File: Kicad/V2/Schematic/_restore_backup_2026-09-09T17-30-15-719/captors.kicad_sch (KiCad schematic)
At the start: 7 parts, among them U2 TXS0104E

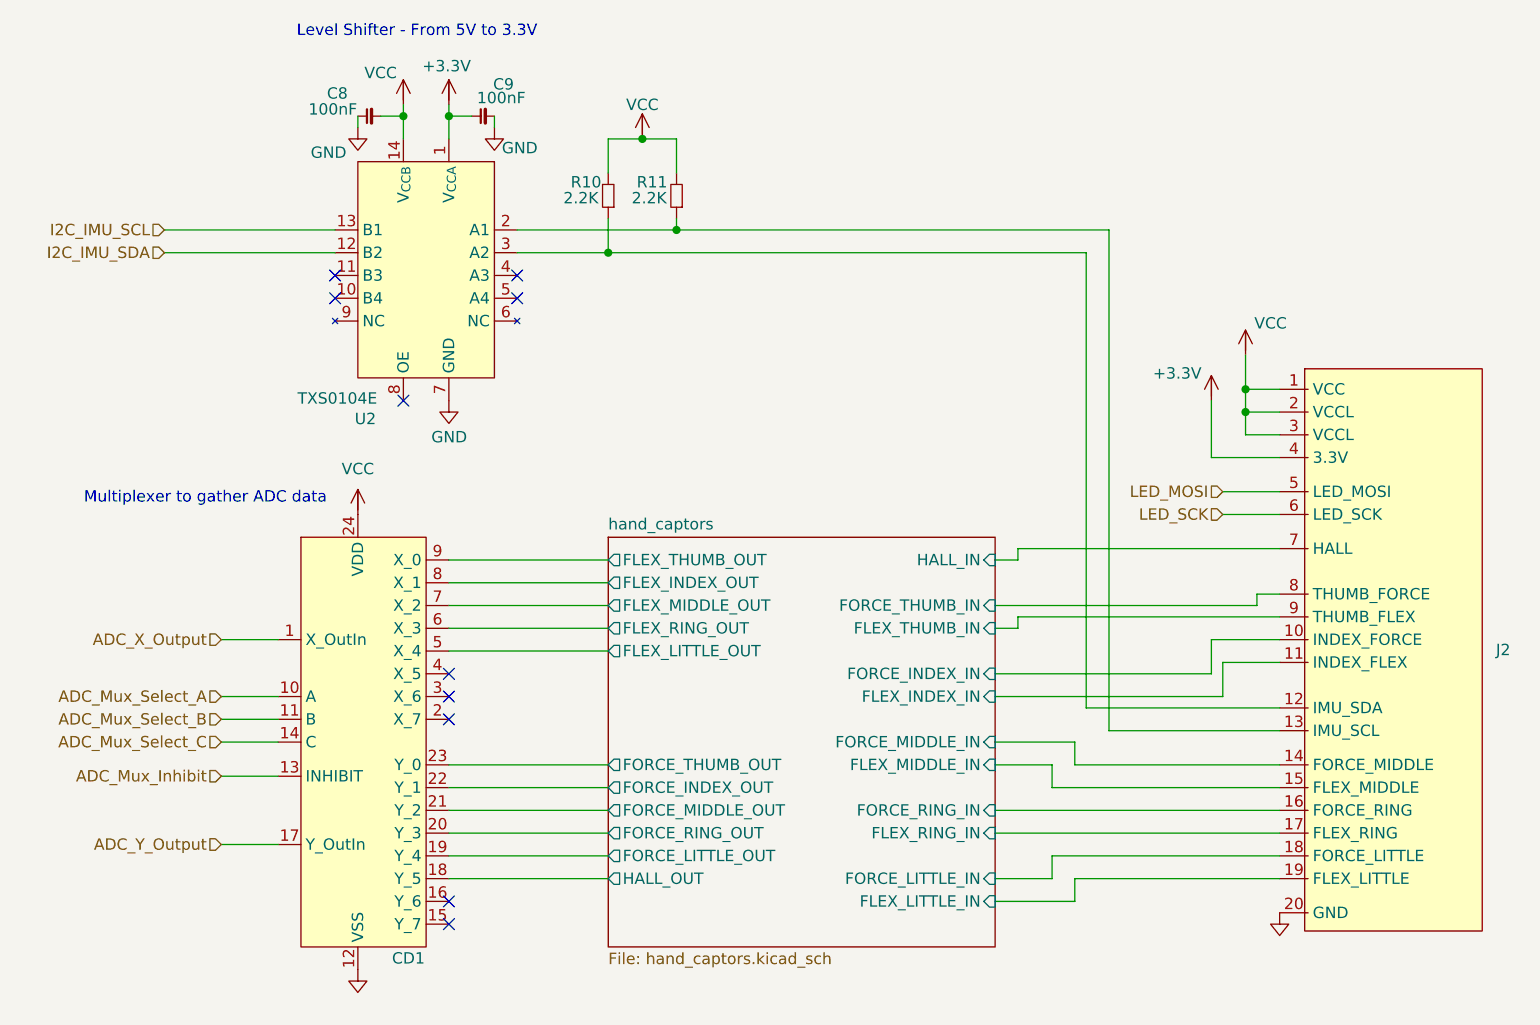
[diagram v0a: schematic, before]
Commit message: finition schematic de reference
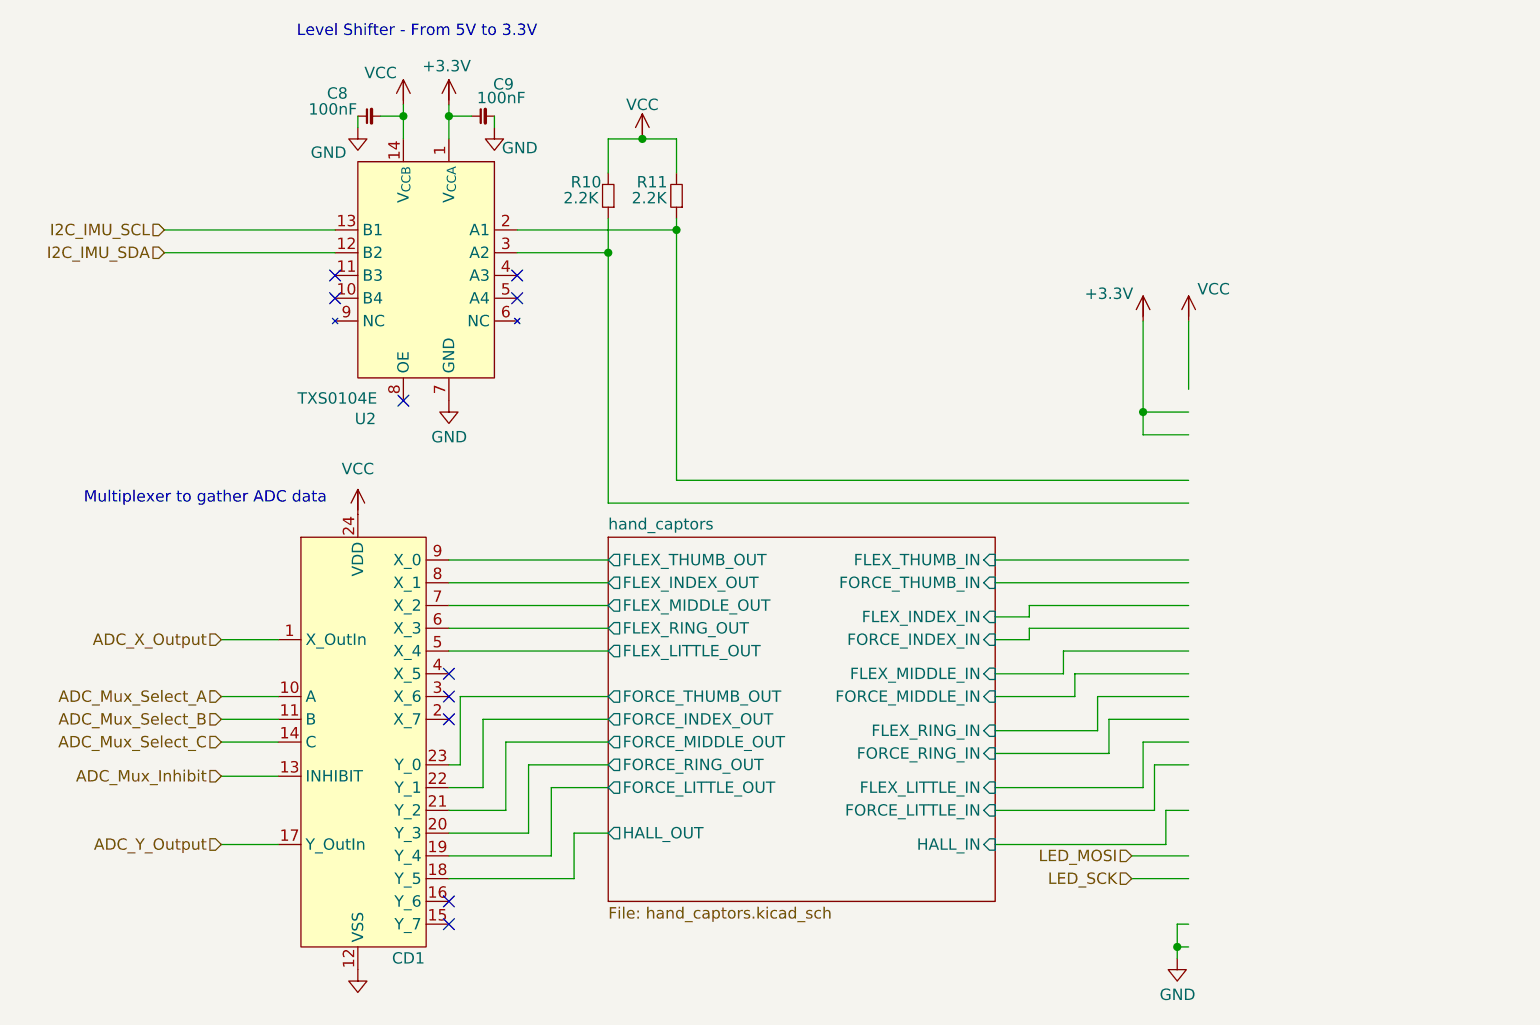
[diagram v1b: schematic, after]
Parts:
- removed J2: (no value), symbol G-Love:FPC_CONNECTOR
